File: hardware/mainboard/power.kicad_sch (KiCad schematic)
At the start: 52 parts

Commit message: ERC fixes
Signed-off-by: gatecat <gatecat@ds0.me>
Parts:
- removed C?: 47µ, symbol Device:CP_Small
- added C9: 47µ, symbol Device:C_Polarized_Small
- gave numbers to parts that had none: 51
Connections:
- net GND: now also C9.2
- net VBUS: now also C9.1

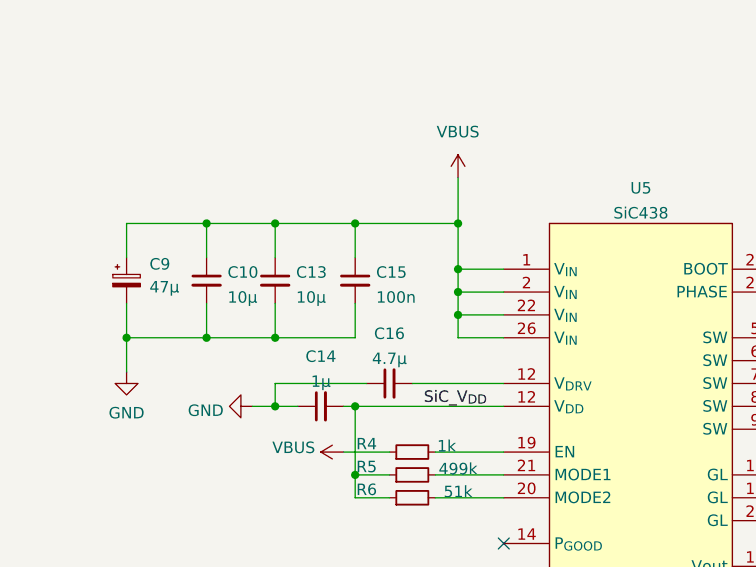
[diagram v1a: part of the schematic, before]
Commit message: Add some footprint mappings
Signed-off-by: gatecat <gatecat@ds0.me>
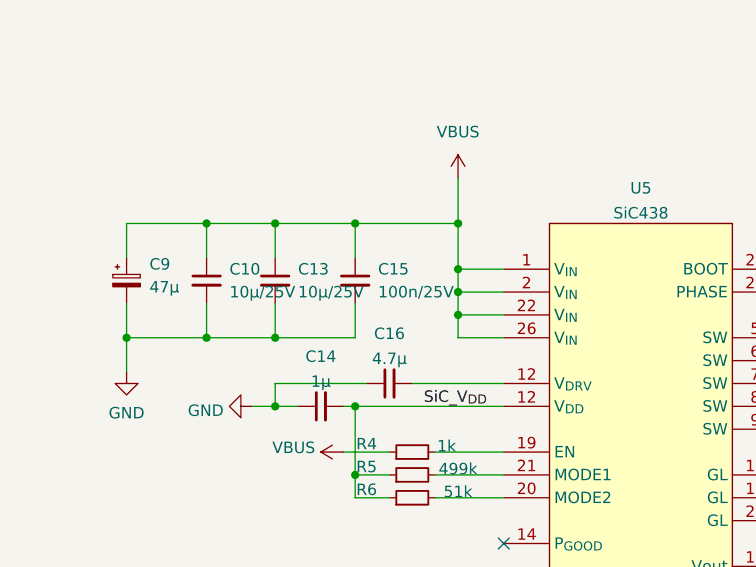
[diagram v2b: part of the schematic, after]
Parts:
- C10: value 10µ -> 10µ/25V; footprint (none) -> Capacitor_SMD:C_1206_3216Metric
- C11, C12, C27, C28: footprint Capacitor_SMD:C_0805_2012Metric -> Capacitor_SMD:C_1206_3216Metric
- C13: value 10µ -> 10µ/25V
- C15: value 100n -> 100n/25V
- C24, C25, C26: footprint (none) -> Capacitor_SMD:C_1206_3216Metric
- C9: footprint (none) -> Capacitor_SMD:CP_Elec_6.3x3.9
- R11, R12, R13, R4, R5, R6: footprint (none) -> Resistor_SMD:R_0402_1005Metric
- U5: footprint (none) -> meowality:MLP44-24L
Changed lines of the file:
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@@
       (effects (font (size 1.27 1.27)) (justify left))
     )
-    (property "Footprint" "" (id 2) (at 40.64 128.27 0)
+    (property "Footprint" "Capacitor_SMD:CP_Elec_6.3x3.9" (id 2) (at 40.64 128.27 0)
       (effects (font (size 1.27 1.27)) hide)
     )
@@
   (symbol (lib_id "Device:C_Small") (at 49.53 128.27 0) (unit 1)
     (in_bom yes) (on_board yes) (fields_autoplaced)
-    (property "Reference" "C10" (id 0) (at 51.8541 127.3615 0)
-      (effects (font (size 1.27 1.27)) (justify left))
-    )
-    (property "Value" "10µ" (id 1) (at 51.8541 130.1366 0)
-      (effects (font (size 1.27 1.27)) (justify left))
-    )
-    (property "Footprint" "" (id 2) (at 49.53 128.27 0)
+    (property "Reference" "C10" (id 0) (at 52.07 127.0062 0)
+      (effects (font (size 1.27 1.27)) (justify left))
+    )
+    (property "Value" "10µ/25V" (id 1) (at 52.07 129.5462 0)
+      (effects (font (size 1.27 1.27)) (justify left))
+    )
+    (property "Footprint" "Capacitor_SMD:C_1206_3216Metric" (id 2) (at 49.53 128.27 0)
       (effects (font (size 1.27 1.27)) hide)
     )
@@
   (symbol (lib_id "Device:C_Small") (at 66.04 128.27 0) (unit 1)
     (in_bom yes) (on_board yes) (fields_autoplaced)
-    (property "Reference" "C15" (id 0) (at 68.3641 127.3615 0)
-      (effects (font (size 1.27 1.27)) (justify left))
-    )
-    (property "Value" "100n" (id 1) (at 68.3641 130.1366 0)
+    (property "Reference" "C15" (id 0) (at 68.58 127.0062 0)
+      (effects (font (size 1.27 1.27)) (justify left))
+    )
+    (property "Value" "100n/25V" (id 1) (at 68.58 129.5462 0)
       (effects (font (size 1.27 1.27)) (justify left))
     )
@@
       (effects (font (size 1.27 1.27)) (justify left))
     )
-    (property "Footprint" "Capacitor_SMD:C_0805_2012Metric" (id 2) (at 170.18 67.31 0)
+    (property "Footprint" "Capacitor_SMD:C_1206_3216Metric" (id 2) (at 170.18 67.31 0)
       (effects (font (size 1.27 1.27)) hide)
     )
@@
       (effects (font (size 1.27 1.27)) (justify left))
     )
-    (property "Footprint" "Capacitor_SMD:C_0805_2012Metric" (id 2) (at 57.15 31.75 0)
+    (property "Footprint" "Capacitor_SMD:C_1206_3216Metric" (id 2) (at 57.15 31.75 0)
       (effects (font (size 1.27 1.27)) hide)
     )
@@
       (effects (font (size 1.27 1.27)) (justify left))
     )
-    (property "Footprint" "" (id 2) (at 153.67 144.78 0)
+    (property "Footprint" "Capacitor_SMD:C_1206_3216Metric" (id 2) (at 153.67 144.78 0)
       (effects (font (size 1.27 1.27)) hide)
     )
@@
       (effects (font (size 1.27 1.27)) (justify left))
     )
-    (property "Footprint" "" (id 2) (at 124.46 158.75 0)
+    (property "Footprint" "Resistor_SMD:R_0402_1005Metric" (id 2) (at 124.46 158.75 0)
       (effects (font (size 1.27 1.27)) hide)
     )
@@
     (property "Reference" "U5" (id 0) (at 97.79 118.0043 0))
     (property "Value" "SiC438" (id 1) (at 97.79 120.7794 0))
-    (property "Footprint" "" (id 2) (at 97.79 172.72 0)
+    (property "Footprint" "meowality:MLP44-24L" (id 2) (at 97.79 172.72 0)
       (effects (font (size 1.27 1.27)) hide)
     )
@@
       (effects (font (size 1.27 1.27)) (justify left))
     )
-    (property "Footprint" "Capacitor_SMD:C_0805_2012Metric" (id 2) (at 170.18 31.75 0)
+    (property "Footprint" "Capacitor_SMD:C_1206_3216Metric" (id 2) (at 170.18 31.75 0)
       (effects (font (size 1.27 1.27)) hide)
     )
@@
       (effects (font (size 1.27 1.27)) (justify left))
     )
-    (property "Footprint" "" (id 2) (at 124.46 151.13 0)
+    (property "Footprint" "Resistor_SMD:R_0402_1005Metric" (id 2) (at 124.46 151.13 0)
       (effects (font (size 1.27 1.27)) hide)
     )
@@
     (property "Reference" "R6" (id 0) (at 67.31 151.5069 90))
     (property "Value" "51k" (id 1) (at 77.47 151.742 90))
-    (property "Footprint" "" (id 2) (at 72.39 152.4 0)
+    (property "Footprint" "Resistor_SMD:R_0402_1005Metric" (id 2) (at 72.39 152.4 0)
       (effects (font (size 1.27 1.27)) hide)
     )
@@
   (symbol (lib_id "Device:C_Small") (at 57.15 128.27 0) (unit 1)
     (in_bom yes) (on_board yes) (fields_autoplaced)
-    (property "Reference" "C13" (id 0) (at 59.4741 127.3615 0)
-      (effects (font (size 1.27 1.27)) (justify left))
-    )
-    (property "Value" "10µ" (id 1) (at 59.4741 130.1366 0)
+    (property "Reference" "C13" (id 0) (at 59.69 127.0062 0)
+      (effects (font (size 1.27 1.27)) (justify left))
+    )
+    (property "Value" "10µ/25V" (id 1) (at 59.69 129.5462 0)
       (effects (font (size 1.27 1.27)) (justify left))
     )
@@
     (property "Reference" "R13" (id 0) (at 128.27 122.2969 90))
     (property "Value" "2.2" (id 1) (at 128.27 125.072 90))
-    (property "Footprint" "" (id 2) (at 128.27 127 0)
+    (property "Footprint" "Resistor_SMD:R_0402_1005Metric" (id 2) (at 128.27 127 0)
       (effects (font (size 1.27 1.27)) hide)
     )
@@
       (effects (font (size 1.27 1.27)) (justify left))
     )
-    (property "Footprint" "Capacitor_SMD:C_0805_2012Metric" (id 2) (at 57.15 67.31 0)
+    (property "Footprint" "Capacitor_SMD:C_1206_3216Metric" (id 2) (at 57.15 67.31 0)
       (effects (font (size 1.27 1.27)) hide)
     )
@@
     (property "Reference" "R5" (id 0) (at 67.31 148.9669 90))
     (property "Value" "499k" (id 1) (at 77.47 149.202 90))
-    (property "Footprint" "" (id 2) (at 72.39 149.86 0)
+    (property "Footprint" "Resistor_SMD:R_0402_1005Metric" (id 2) (at 72.39 149.86 0)
       (effects (font (size 1.27 1.27)) hide)
     )
@@
       (effects (font (size 1.27 1.27)) (justify left))
     )
-    (property "Footprint" "" (id 2) (at 138.43 144.78 0)
+    (property "Footprint" "Capacitor_SMD:C_1206_3216Metric" (id 2) (at 138.43 144.78 0)
       (effects (font (size 1.27 1.27)) hide)
     )
@@
       (effects (font (size 1.27 1.27)) (justify left))
     )
-    (property "Footprint" "" (id 2) (at 146.05 144.78 0)
+    (property "Footprint" "Capacitor_SMD:C_1206_3216Metric" (id 2) (at 146.05 144.78 0)
       (effects (font (size 1.27 1.27)) hide)
     )
@@
     (property "Reference" "R4" (id 0) (at 67.31 146.4269 90))
     (property "Value" "1k" (id 1) (at 76.2 146.662 90))
-    (property "Footprint" "" (id 2) (at 72.39 147.32 0)
-      (effects (font (size 1.27 1.27)) hide)
-    )
+    (property "Footprint" "Resistor_SMD:R_0402_1005Metric" (id 2) (at 72.39 147.32 0)
+      (effects (font (size 1.27 1.27)) hide)
+    )

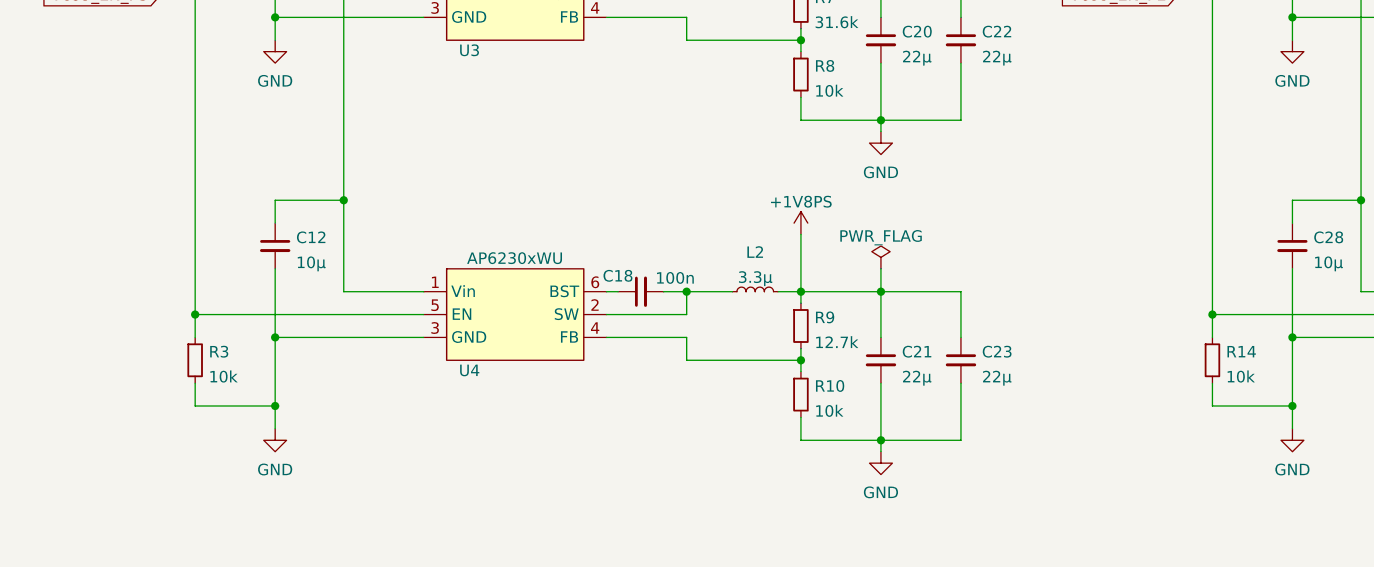
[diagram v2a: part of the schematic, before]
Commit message: Footprint assignments and related fixes
Signed-off-by: gatecat <gatecat@ds0.me>
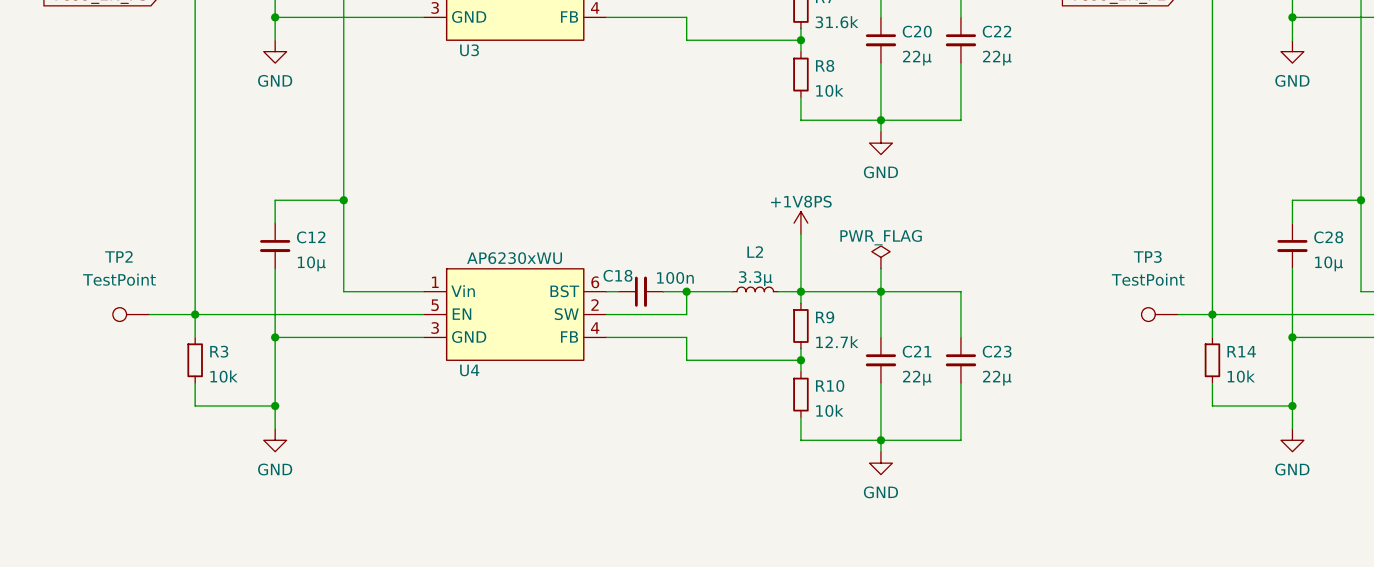
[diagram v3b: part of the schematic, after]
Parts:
- added TP2, TP3: TestPoint, TestPoint:TestPoint_Pad_D2.0mm, symbol Connector:TestPoint
- C13: footprint (none) -> Capacitor_SMD:C_1206_3216Metric
- C14, C16: footprint (none) -> Capacitor_SMD:C_0603_1608Metric
- C15: footprint (none) -> Capacitor_SMD:C_0805_2012Metric
- C19: footprint (none) -> Capacitor_SMD:C_0402_1005Metric
- L3: footprint (none) -> Inductor_SMD:L_Bourns_SRP7028A_7.3x6.6mm
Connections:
- net VccO_EN_PL: now also TP3.1
- net VccO_EN_PS: now also TP2.1
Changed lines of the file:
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@@
+    (stroke (width 0) (type default) (color 0 0 0 0))
+  )
+  (wire (pts (xy 157.48 74.93) (xy 161.29 74.93))
     (stroke (width 0) (type default) (color 0 0 0 0))
   )
@@
   )
   (wire (pts (xy 48.26 85.09) (xy 57.15 85.09))
+    (stroke (width 0) (type default) (color 0 0 0 0))
+  )
+  (wire (pts (xy 43.18 74.93) (xy 48.26 74.93))
     (stroke (width 0) (type default) (color 0 0 0 0))
   )
@@
     (property "Reference" "C19" (id 0) (at 120.65 121.4714 90))
     (property "Value" "100n" (id 1) (at 120.65 124.2465 90))
-    (property "Footprint" "" (id 2) (at 120.65 127 0)
+    (property "Footprint" "Capacitor_SMD:C_0402_1005Metric" (id 2) (at 120.65 127 0)
       (effects (font (size 1.27 1.27)) hide)
     )
@@
       (effects (font (size 1.27 1.27)) (justify left))
     )
-    (property "Footprint" "" (id 2) (at 66.04 128.27 0)
+    (property "Footprint" "Capacitor_SMD:C_0805_2012Metric" (id 2) (at 66.04 128.27 0)
       (effects (font (size 1.27 1.27)) hide)
     )
@@
     (property "Reference" "C16" (id 0) (at 69.85 134.1714 90))
     (property "Value" "4.7µ" (id 1) (at 69.85 136.9465 90))
-    (property "Footprint" "" (id 2) (at 69.85 139.7 0)
+    (property "Footprint" "Capacitor_SMD:C_0603_1608Metric" (id 2) (at 69.85 139.7 0)
       (effects (font (size 1.27 1.27)) hide)
     )
@@
     (property "Reference" "L3" (id 0) (at 127 135.2254 90))
     (property "Value" "1.5µH" (id 1) (at 127 138.0005 90))
-    (property "Footprint" "" (id 2) (at 127 139.7 0)
+    (property "Footprint" "Inductor_SMD:L_Bourns_SRP7028A_7.3x6.6mm" (id 2) (at 127 139.7 0)
       (effects (font (size 1.27 1.27)) hide)
     )
@@
       (effects (font (size 1.27 1.27)) (justify left))
     )
-    (property "Footprint" "" (id 2) (at 57.15 128.27 0)
+    (property "Footprint" "Capacitor_SMD:C_1206_3216Metric" (id 2) (at 57.15 128.27 0)
       (effects (font (size 1.27 1.27)) hide)
     )
@@
     (pin "2")
   )
+  (symbol (lib_id "Connector:TestPoint") (at 157.48 74.93 90) (unit 1)
+    (in_bom yes) (on_board yes) (fields_autoplaced)
+    (property "Reference" "TP3" (id 0) (at 154.178 68.58 90))
+    (property "Value" "TestPoint" (id 1) (at 154.178 71.12 90))
+    (property "Footprint" "TestPoint:TestPoint_Pad_D2.0mm" (id 2) (at 157.48 69.85 0)
+      (effects (font (size 1.27 1.27)) hide)
+    )
+    (property "Datasheet" "~" (id 3) (at 157.48 69.85 0)
+      (effects (font (size 1.27 1.27)) hide)
+    )
+    (pin "1")
+  )
   (symbol (lib_id "Device:C_Small") (at 62.23 142.24 90) (unit 1)
     (in_bom yes) (on_board yes) (fields_autoplaced)
     (property "Reference" "C14" (id 0) (at 62.23 136.7114 90))
     (property "Value" "1µ" (id 1) (at 62.23 139.4865 90))
-    (property "Footprint" "" (id 2) (at 62.23 142.24 0)
+    (property "Footprint" "Capacitor_SMD:C_0603_1608Metric" (id 2) (at 62.23 142.24 0)
       (effects (font (size 1.27 1.27)) hide)
     )
@@
     (pin "2")
   )
+  (symbol (lib_id "Connector:TestPoint") (at 43.18 74.93 90) (unit 1)
+    (in_bom yes) (on_board yes) (fields_autoplaced)
+    (property "Reference" "TP2" (id 0) (at 39.878 68.58 90))
+    (property "Value" "TestPoint" (id 1) (at 39.878 71.12 90))
+    (property "Footprint" "TestPoint:TestPoint_Pad_D2.0mm" (id 2) (at 43.18 69.85 0)
+      (effects (font (size 1.27 1.27)) hide)
+    )
+    (property "Datasheet" "~" (id 3) (at 43.18 69.85 0)
+      (effects (font (size 1.27 1.27)) hide)
+    )
+    (pin "1")
+  )
   (symbol (lib_id "power:GND") (at 57.15 44.45 0) (unit 1)

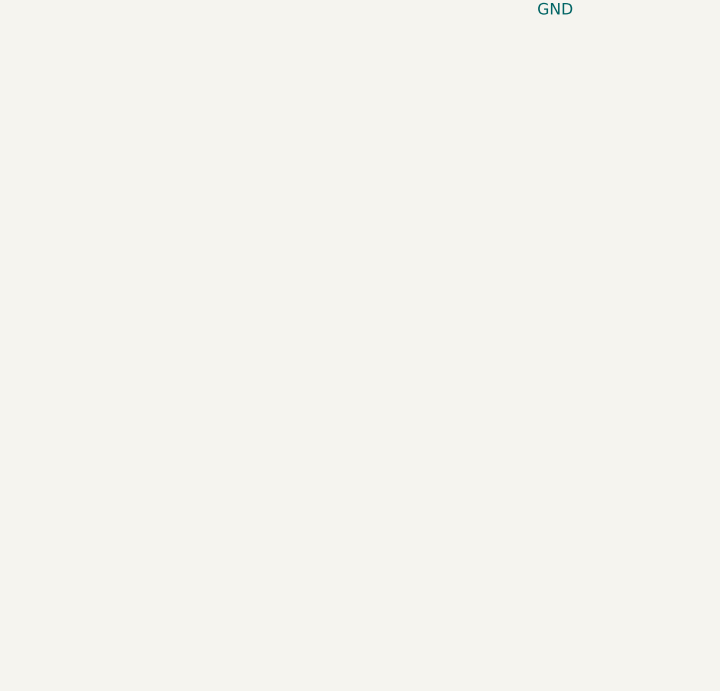
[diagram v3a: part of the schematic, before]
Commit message: Rework power arch to add 3V3PL; 5x PL RGB LEDs
Signed-off-by: gatecat <gatecat@ds0.me>
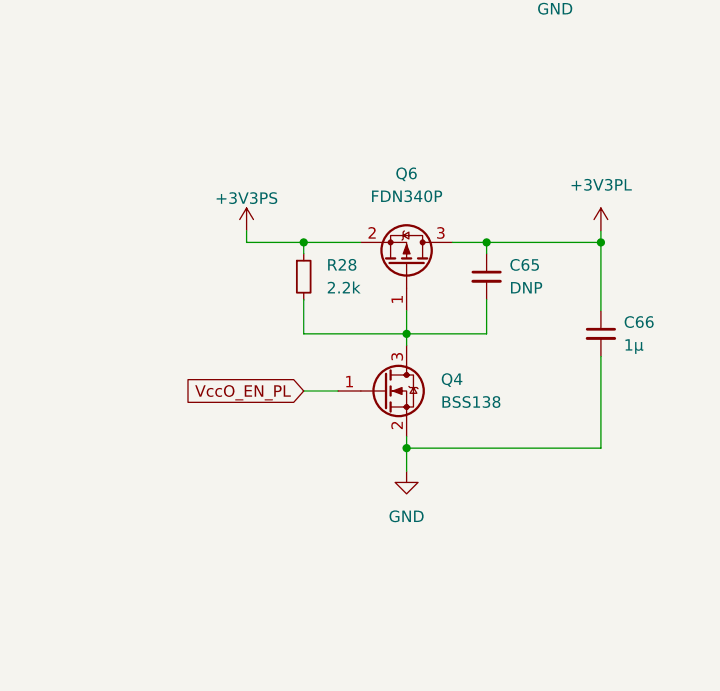
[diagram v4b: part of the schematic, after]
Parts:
- added C65: DNP, symbol Device:C_Small
- added C66: 1µ, symbol Device:C_Small
- added Q4: BSS138, Package_TO_SOT_SMD:SOT-23, symbol Transistor_FET:BSS138
- added Q6: FDN340P, Package_TO_SOT_SMD:SOT-23, symbol Transistor_FET:FDN340P
- added R28: 2.2k, symbol Device:R_Small
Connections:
- net +3V3PS: now also C65.1, C66.1, Q6.2 (S), Q6.3 (D), R28.1
- net GND: now also C66.2, Q4.2 (S)
- net VccO_EN_PL: now also Q4.1 (G)
- new net: C65.2, Q4.3 (D), Q6.1 (G), R28.2

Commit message: Footprint assignment updates
Signed-off-by: gatecat <gatecat@ds0.me>
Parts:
- C65, C66: footprint (none) -> Capacitor_SMD:C_0603_1608Metric
- R28: footprint (none) -> Resistor_SMD:R_0402_1005Metric
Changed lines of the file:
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@@
       (effects (font (size 1.27 1.27)) (justify left))
     )
-    (property "Footprint" "" (id 2) (at 229.87 124.46 0)
+    (property "Footprint" "Capacitor_SMD:C_0603_1608Metric" (id 2) (at 229.87 124.46 0)
       (effects (font (size 1.27 1.27)) hide)
     )
@@
       (effects (font (size 1.27 1.27)) (justify left))
     )
-    (property "Footprint" "" (id 2) (at 242.57 130.81 0)
+    (property "Footprint" "Capacitor_SMD:C_0603_1608Metric" (id 2) (at 242.57 130.81 0)
       (effects (font (size 1.27 1.27)) hide)
     )
@@
       (effects (font (size 1.27 1.27)) (justify left))
     )
-    (property "Footprint" "" (id 2) (at 209.55 124.46 0)
+    (property "Footprint" "Resistor_SMD:R_0402_1005Metric" (id 2) (at 209.55 124.46 0)
       (effects (font (size 1.27 1.27)) hide)
     )
